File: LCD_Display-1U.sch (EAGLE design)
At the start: 4 parts, among them U1 NEWHAVEN_LCD

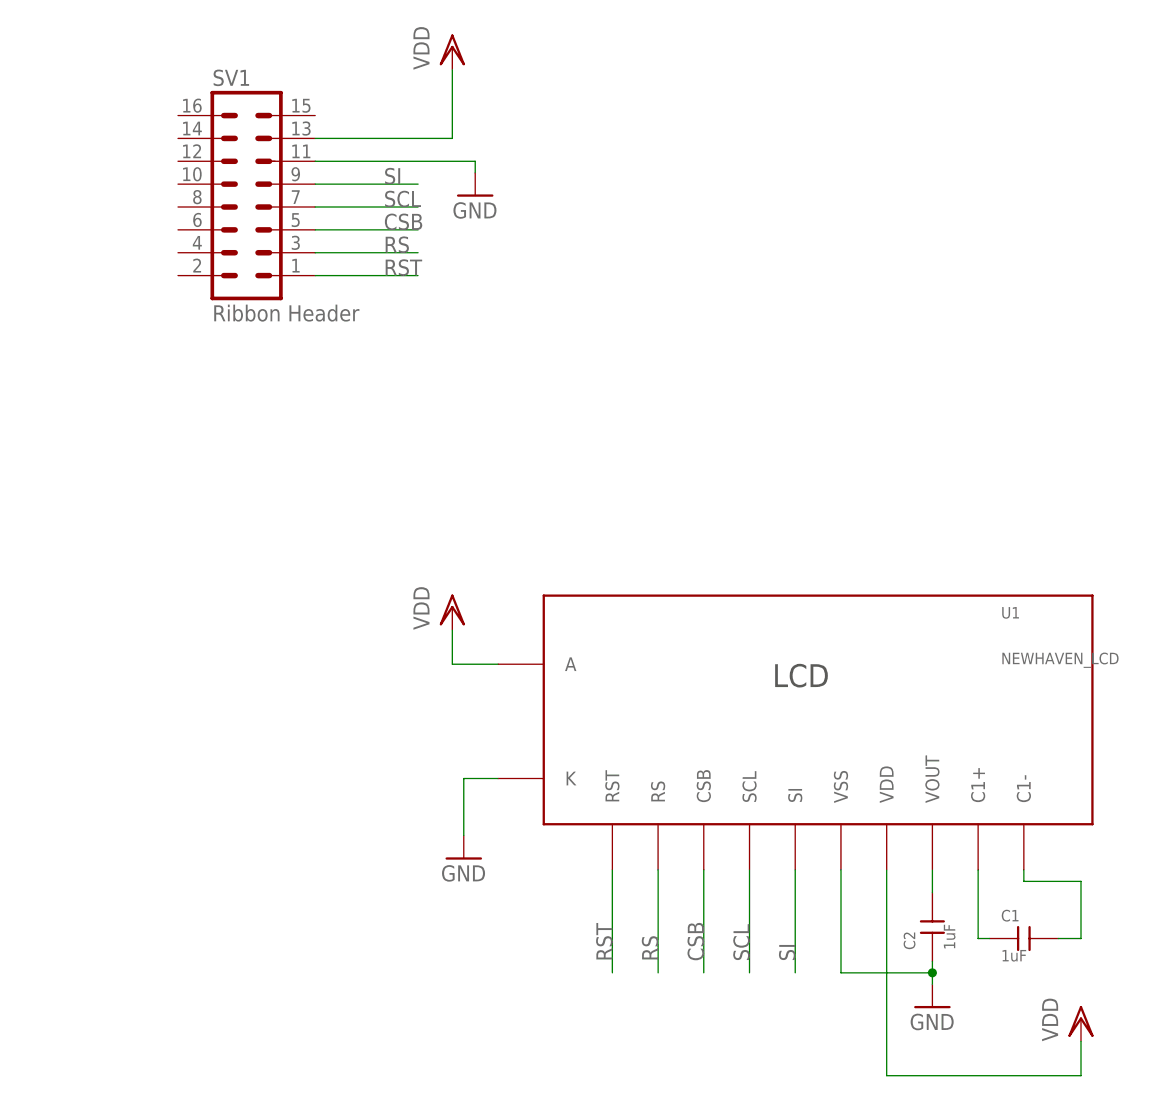
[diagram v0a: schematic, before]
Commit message: Modified LCD-1U for production run; added 8 pin ribbon connector
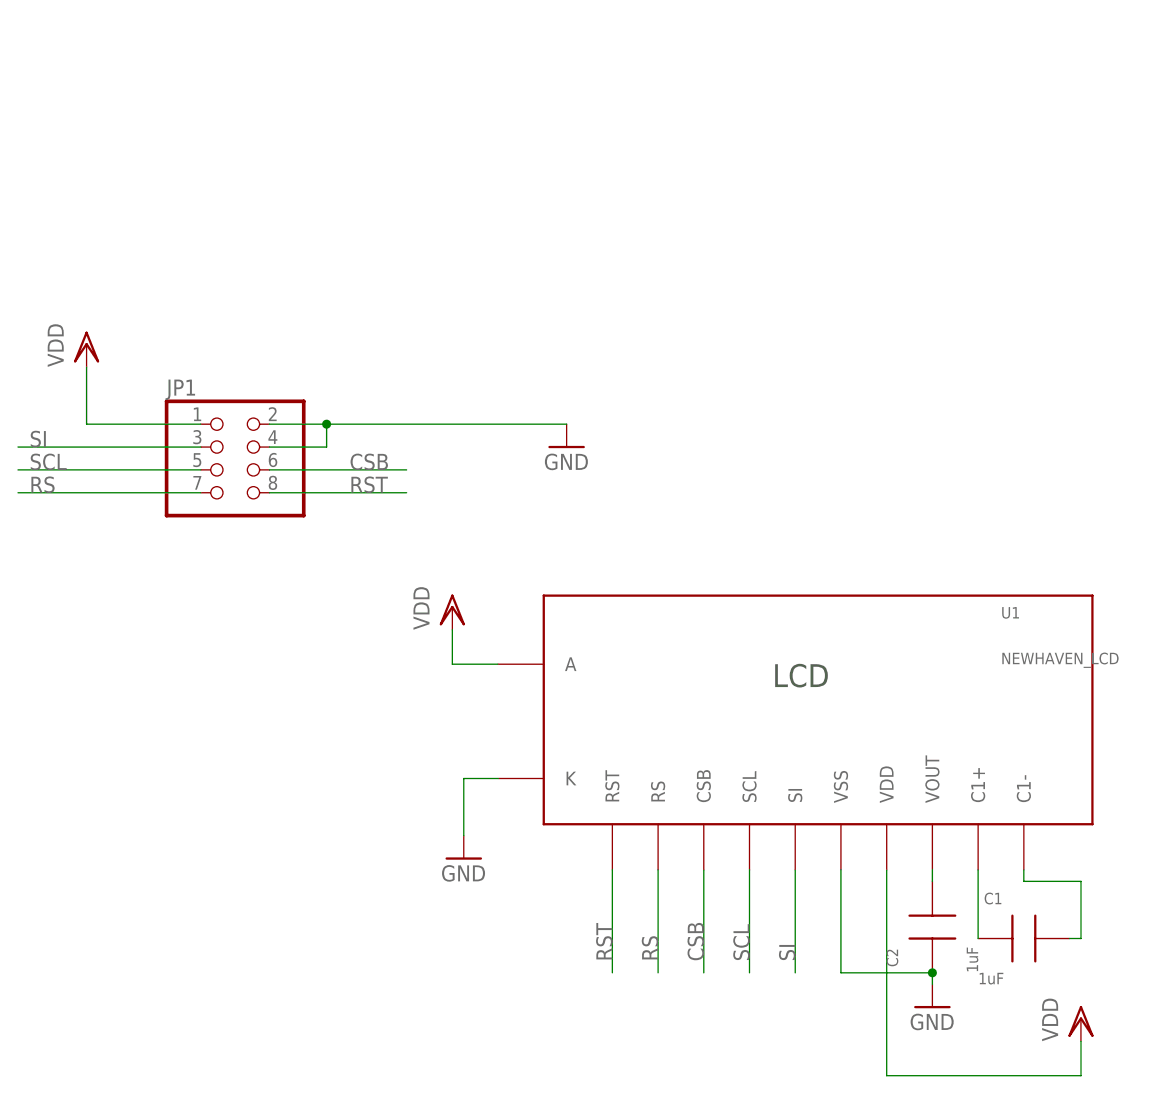
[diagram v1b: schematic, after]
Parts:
- removed SV1: Ribbon Header, mcu-accessories:ML16
- added JP1: (no value), mcu-accessories:PINHD-2X4SMT
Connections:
- net CSB: now also JP1.6; no longer SV1.5
- net GND: now also JP1.2, JP1.4; no longer SV1.11
- net RS: now also JP1.7; no longer SV1.3
- net RST: now also JP1.8; no longer SV1.1
- net SCL: now also JP1.5; no longer SV1.7
- net SI: now also JP1.3; no longer SV1.9
- net VDD: now also JP1.1; no longer SV1.13
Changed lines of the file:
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@@
 <?xml version="1.0" encoding="utf-8"?>
 <!DOCTYPE eagle SYSTEM "eagle.dtd">
-<eagle version="6.5.0">
+<eagle version="6.6.0">
 <drawing>
 <settings>
@@
 <parts>
 <part name="U1" library="mcu-accessories" deviceset="NEWHAVEN_LCD" device=""/>
-<part name="SV1" library="mcu-accessories" deviceset="ML16" device="" value="Ribbon Header">
-<attribute name="PARTNO" value="S9171-ND"/>
-</part>
 <part name="C1" library="rlc-jqi" deviceset="CAP" device="0805" value="1uF">
 <attribute name="PARTNO" value="1276-2396-1-ND"/>
@@
 <part name="VDD1" library="supply1" deviceset="VDD" device=""/>
 <part name="VDD2" library="supply1" deviceset="VDD" device=""/>
-<part name="VDD3" library="supply1" deviceset="VDD" device=""/>
-<part name="GND3" library="supply1" deviceset="GND" device=""/>
+<part name="JP1" library="mcu-accessories" deviceset="PINHD-2X4" device="SMT"/>
+<part name="VDD4" library="supply1" deviceset="VDD" device=""/>
+<part name="GND4" library="supply1" deviceset="GND" device=""/>
 </parts>
 <sheets>
@@
 <instances>
 <instance part="U1" gate="G$1" x="68.58" y="59.69"/>
-<instance part="SV1" gate="1" x="2.54" y="118.11">
-<attribute name="PARTNO" x="2.54" y="118.11" size="1.778" layer="96" display="off"/>
-</instance>
 <instance part="C1" gate="G$1" x="88.9" y="34.29">
 <attribute name="PARTNO" x="88.9" y="34.29" size="1.778" layer="96" display="off"/>
@@
 <instance part="VDD1" gate="G$1" x="25.4" y="71.12"/>
 <instance part="VDD2" gate="G$1" x="95.25" y="25.4"/>
-<instance part="VDD3" gate="G$1" x="25.4" y="133.35"/>
-<instance part="GND3" gate="1" x="27.94" y="116.84"/>
+<instance part="JP1" gate="A" x="0" y="86.36"/>
+<instance part="VDD4" gate="G$1" x="-15.24" y="100.33"/>
+<instance part="GND4" gate="1" x="38.1" y="88.9"/>
 </instances>
 <busses>
@@
 <wire x1="83.82" y1="41.91" x2="83.82" y2="34.29" width="0.1524" layer="91"/>
 <pinref part="C1" gate="G$1" pin="P$1"/>
-<wire x1="83.82" y1="34.29" x2="85.09" y2="34.29" width="0.1524" layer="91"/>
 </segment>
 </net>
@@
 <segment>
 <pinref part="C1" gate="G$1" pin="P$2"/>
-<wire x1="92.71" y1="34.29" x2="95.25" y2="34.29" width="0.1524" layer="91"/>
+<wire x1="93.98" y1="34.29" x2="95.25" y2="34.29" width="0.1524" layer="91"/>
 <wire x1="95.25" y1="34.29" x2="95.25" y2="40.64" width="0.1524" layer="91"/>
 <pinref part="U1" gate="G$1" pin="C1-"/>
@@
 <pinref part="C2" gate="G$1" pin="P$2"/>
 <pinref part="U1" gate="G$1" pin="VOUT"/>
-<wire x1="78.74" y1="39.37" x2="78.74" y2="41.91" width="0.1524" layer="91"/>
+<wire x1="78.74" y1="40.64" x2="78.74" y2="41.91" width="0.1524" layer="91"/>
 </segment>
 </net>
@@
 <wire x1="78.74" y1="29.21" x2="78.74" y2="30.48" width="0.1524" layer="91"/>
 <pinref part="U1" gate="G$1" pin="VSS"/>
-<wire x1="78.74" y1="30.48" x2="78.74" y2="31.75" width="0.1524" layer="91"/>
 <wire x1="68.58" y1="41.91" x2="68.58" y2="30.48" width="0.1524" layer="91"/>
 <wire x1="68.58" y1="30.48" x2="78.74" y2="30.48" width="0.1524" layer="91"/>
@@
 </segment>
 <segment>
-<pinref part="SV1" gate="1" pin="11"/>
-<wire x1="10.16" y1="120.65" x2="27.94" y2="120.65" width="0.1524" layer="91"/>
-<pinref part="GND3" gate="1" pin="GND"/>
-<wire x1="27.94" y1="120.65" x2="27.94" y2="119.38" width="0.1524" layer="91"/>
+<pinref part="JP1" gate="A" pin="2"/>
+<pinref part="GND4" gate="1" pin="GND"/>
+<wire x1="5.08" y1="91.44" x2="11.43" y2="91.44" width="0.1524" layer="91"/>
+<pinref part="JP1" gate="A" pin="4"/>
+<wire x1="11.43" y1="91.44" x2="38.1" y2="91.44" width="0.1524" layer="91"/>
+<wire x1="5.08" y1="88.9" x2="11.43" y2="88.9" width="0.1524" layer="91"/>
+<wire x1="11.43" y1="88.9" x2="11.43" y2="91.44" width="0.1524" layer="91"/>
+<junction x="11.43" y="91.44"/>
 </segment>
 </net>
@@
 </segment>
 <segment>
-<pinref part="SV1" gate="1" pin="13"/>
-<wire x1="10.16" y1="123.19" x2="25.4" y2="123.19" width="0.1524" layer="91"/>
-<pinref part="VDD3" gate="G$1" pin="VDD"/>
-<wire x1="25.4" y1="123.19" x2="25.4" y2="130.81" width="0.1524" layer="91"/>
+<pinref part="VDD4" gate="G$1" pin="VDD"/>
+<wire x1="-15.24" y1="97.79" x2="-15.24" y2="91.44" width="0.1524" layer="91"/>
+<pinref part="JP1" gate="A" pin="1"/>
+<wire x1="-15.24" y1="91.44" x2="-2.54" y2="91.44" width="0.1524" layer="91"/>
 </segment>
 </net>
@@
 </segment>
 <segment>
-<pinref part="SV1" gate="1" pin="9"/>
-<wire x1="10.16" y1="118.11" x2="21.59" y2="118.11" width="0.1524" layer="91"/>
-<label x="17.78" y="118.11" size="1.778" layer="95"/>
+<pinref part="JP1" gate="A" pin="3"/>
+<wire x1="-2.54" y1="88.9" x2="-22.86" y2="88.9" width="0.1524" layer="91"/>
+<label x="-21.59" y="88.9" size="1.778" layer="95"/>
 </segment>
 </net>
@@
 </segment>
 <segment>
-<pinref part="SV1" gate="1" pin="7"/>
-<wire x1="10.16" y1="115.57" x2="21.59" y2="115.57" width="0.1524" layer="91"/>
-<label x="17.78" y="115.57" size="1.778" layer="95"/>
+<pinref part="JP1" gate="A" pin="5"/>
+<wire x1="-2.54" y1="86.36" x2="-22.86" y2="86.36" width="0.1524" layer="91"/>
+<label x="-21.59" y="86.36" size="1.778" layer="95"/>
 </segment>
 </net>
@@
 </segment>
 <segment>
-<pinref part="SV1" gate="1" pin="5"/>
-<wire x1="10.16" y1="113.03" x2="21.59" y2="113.03" width="0.1524" layer="91"/>
-<label x="17.78" y="113.03" size="1.778" layer="95"/>
+<pinref part="JP1" gate="A" pin="6"/>
+<wire x1="5.08" y1="86.36" x2="20.32" y2="86.36" width="0.1524" layer="91"/>
+<label x="13.97" y="86.36" size="1.778" layer="95"/>
 </segment>
 </net>
@@
 </segment>
 <segment>
-<pinref part="SV1" gate="1" pin="3"/>
-<wire x1="10.16" y1="110.49" x2="21.59" y2="110.49" width="0.1524" layer="91"/>
-<label x="17.78" y="110.49" size="1.778" layer="95"/>
+<pinref part="JP1" gate="A" pin="7"/>
+<wire x1="-2.54" y1="83.82" x2="-22.86" y2="83.82" width="0.1524" layer="91"/>
+<label x="-21.59" y="83.82" size="1.778" layer="95"/>
 </segment>
 </net>
@@
 </segment>
 <segment>
-<pinref part="SV1" gate="1" pin="1"/>
-<wire x1="10.16" y1="107.95" x2="21.59" y2="107.95" width="0.1524" layer="91"/>
-<label x="17.78" y="107.95" size="1.778" layer="95"/>
-</segment>
-</net>
+<pinref part="JP1" gate="A" pin="8"/>
+<wire x1="5.08" y1="83.82" x2="20.32" y2="83.82" width="0.1524" layer="91"/>
+<label x="13.97" y="83.82" size="1.778" layer="95"/>
+</segment>
+</net>

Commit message: MacroFab Files
Added files to use Macrofab to get PCBs.

DSB
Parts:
- C1, C2: PARTNO 1276-2396-1-ND -> CL21A105KBCLNNC
- JP1: PARTNO (none) -> 0015912080
- U1: PARTNO (none) -> NHD-C0216CZ-FSW-FBW-3V3
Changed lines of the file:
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@@
 <?xml version="1.0" encoding="utf-8"?>
 <!DOCTYPE eagle SYSTEM "eagle.dtd">
-<eagle version="6.6.0">
+<eagle version="7.7.0">
 <drawing>
 <settings>
@@
 </classes>
 <parts>
-<part name="U1" library="mcu-accessories" deviceset="NEWHAVEN_LCD" device=""/>
+<part name="U1" library="mcu-accessories" deviceset="NEWHAVEN_LCD" device="">
+<attribute name="PARTNO" value="NHD-C0216CZ-FSW-FBW-3V3"/>
+</part>
 <part name="C1" library="rlc-jqi" deviceset="CAP" device="0805" value="1uF">
-<attribute name="PARTNO" value="1276-2396-1-ND"/>
+<attribute name="PARTNO" value="CL21A105KBCLNNC"/>
 </part>
 <part name="C2" library="rlc-jqi" deviceset="CAP" device="0805" value="1uF">
-<attribute name="PARTNO" value="1276-2396-1-ND"/>
+<attribute name="PARTNO" value="CL21A105KBCLNNC"/>
 </part>
 <part name="GND1" library="supply1" deviceset="GND" device=""/>
@@
 <part name="VDD1" library="supply1" deviceset="VDD" device=""/>
 <part name="VDD2" library="supply1" deviceset="VDD" device=""/>
-<part name="JP1" library="mcu-accessories" deviceset="PINHD-2X4" device="SMT"/>
+<part name="JP1" library="mcu-accessories" deviceset="PINHD-2X4" device="SMT">
+<attribute name="PARTNO" value="0015912080"/>
+</part>
 <part name="VDD4" library="supply1" deviceset="VDD" device=""/>
 <part name="GND4" library="supply1" deviceset="GND" device=""/>
@@
 </plain>
 <instances>
-<instance part="U1" gate="G$1" x="68.58" y="59.69"/>
+<instance part="U1" gate="G$1" x="68.58" y="59.69">
+<attribute name="PARTNO" x="68.58" y="59.69" size="1.778" layer="96" display="off"/>
+</instance>
 <instance part="C1" gate="G$1" x="88.9" y="34.29">
 <attribute name="PARTNO" x="88.9" y="34.29" size="1.778" layer="96" display="off"/>
@@
 <instance part="VDD1" gate="G$1" x="25.4" y="71.12"/>
 <instance part="VDD2" gate="G$1" x="95.25" y="25.4"/>
-<instance part="JP1" gate="A" x="0" y="86.36"/>
+<instance part="JP1" gate="A" x="0" y="86.36">
+<attribute name="PARTNO" x="0" y="86.36" size="1.778" layer="96" display="off"/>
+</instance>
 <instance part="VDD4" gate="G$1" x="-15.24" y="100.33"/>
 <instance part="GND4" gate="1" x="38.1" y="88.9"/>
